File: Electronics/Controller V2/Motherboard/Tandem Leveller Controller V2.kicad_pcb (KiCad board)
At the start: 6 copper layers, 230.5 x 129 mm, 75 parts, among them J1 Conn_01x08, J14 TABLET 1 PWR, J15 TABLET 2 PWR, J2 Conn_01x10, J3 GNSS, J4 TERM, J5 Pulse_J0011D01BNL, J6 CAN, J7 Pulse_J0011D01BNL, J8 776180-1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

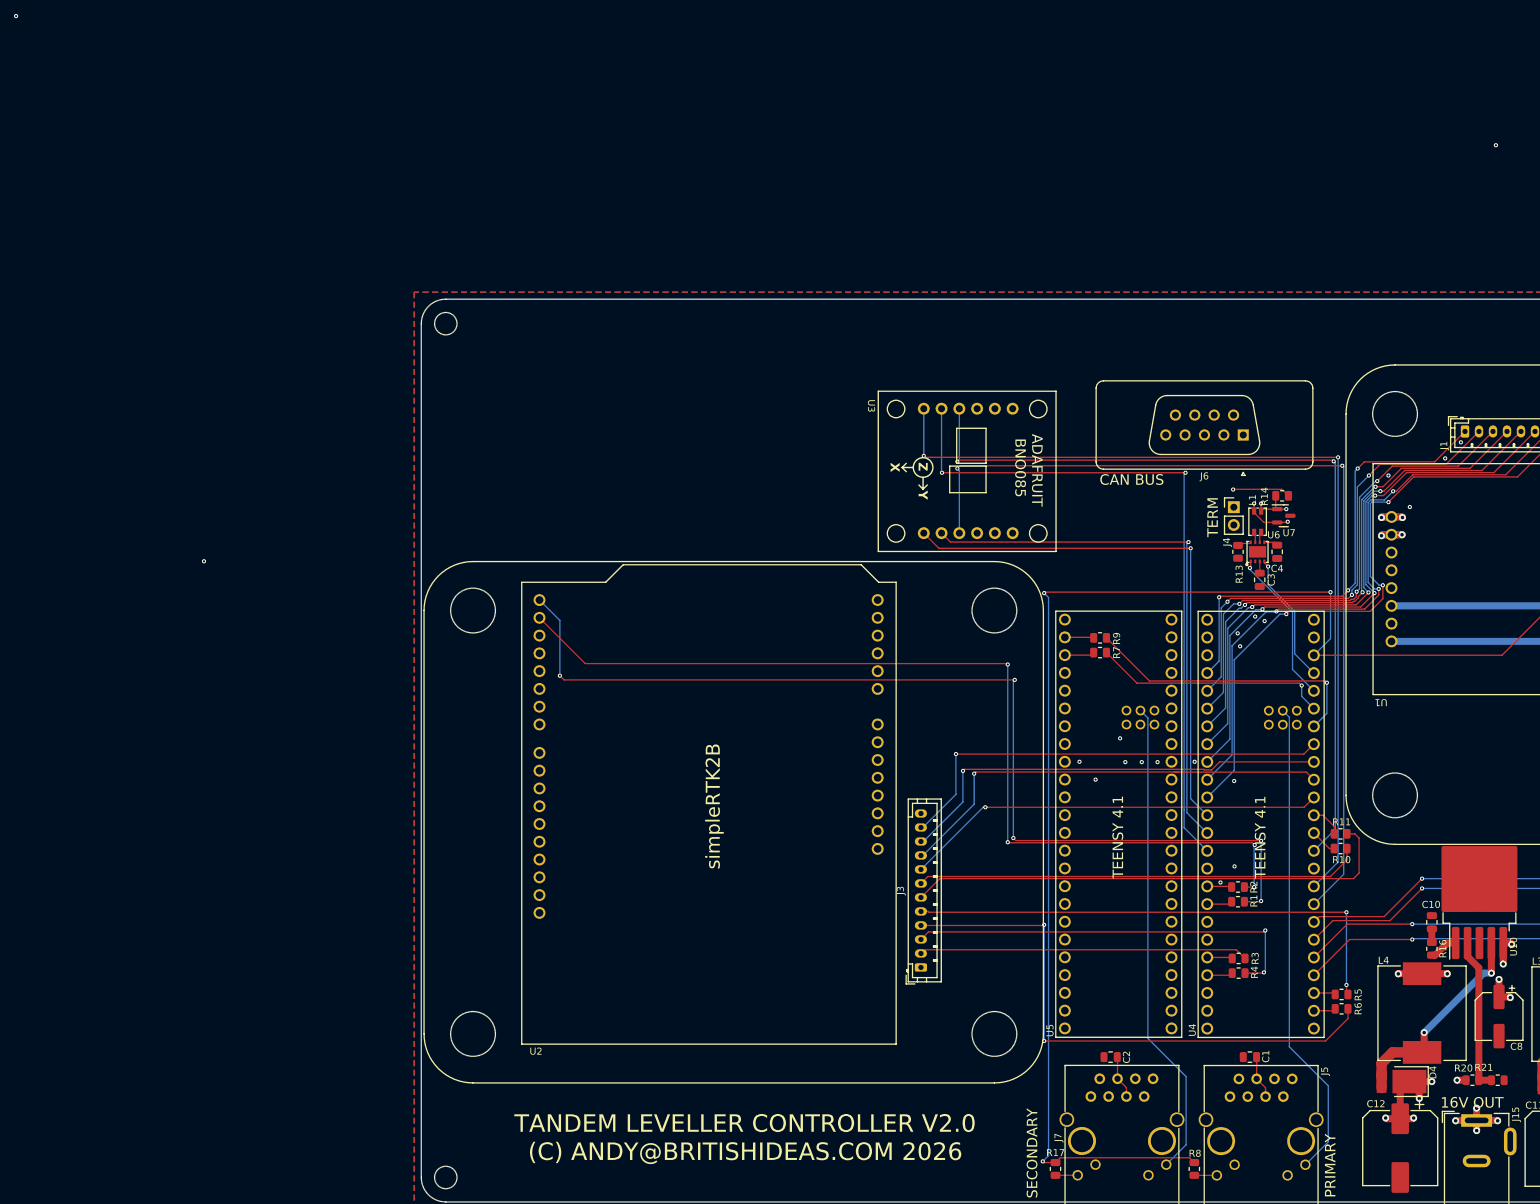
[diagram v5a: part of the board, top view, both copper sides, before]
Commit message: Added generic IMU option.
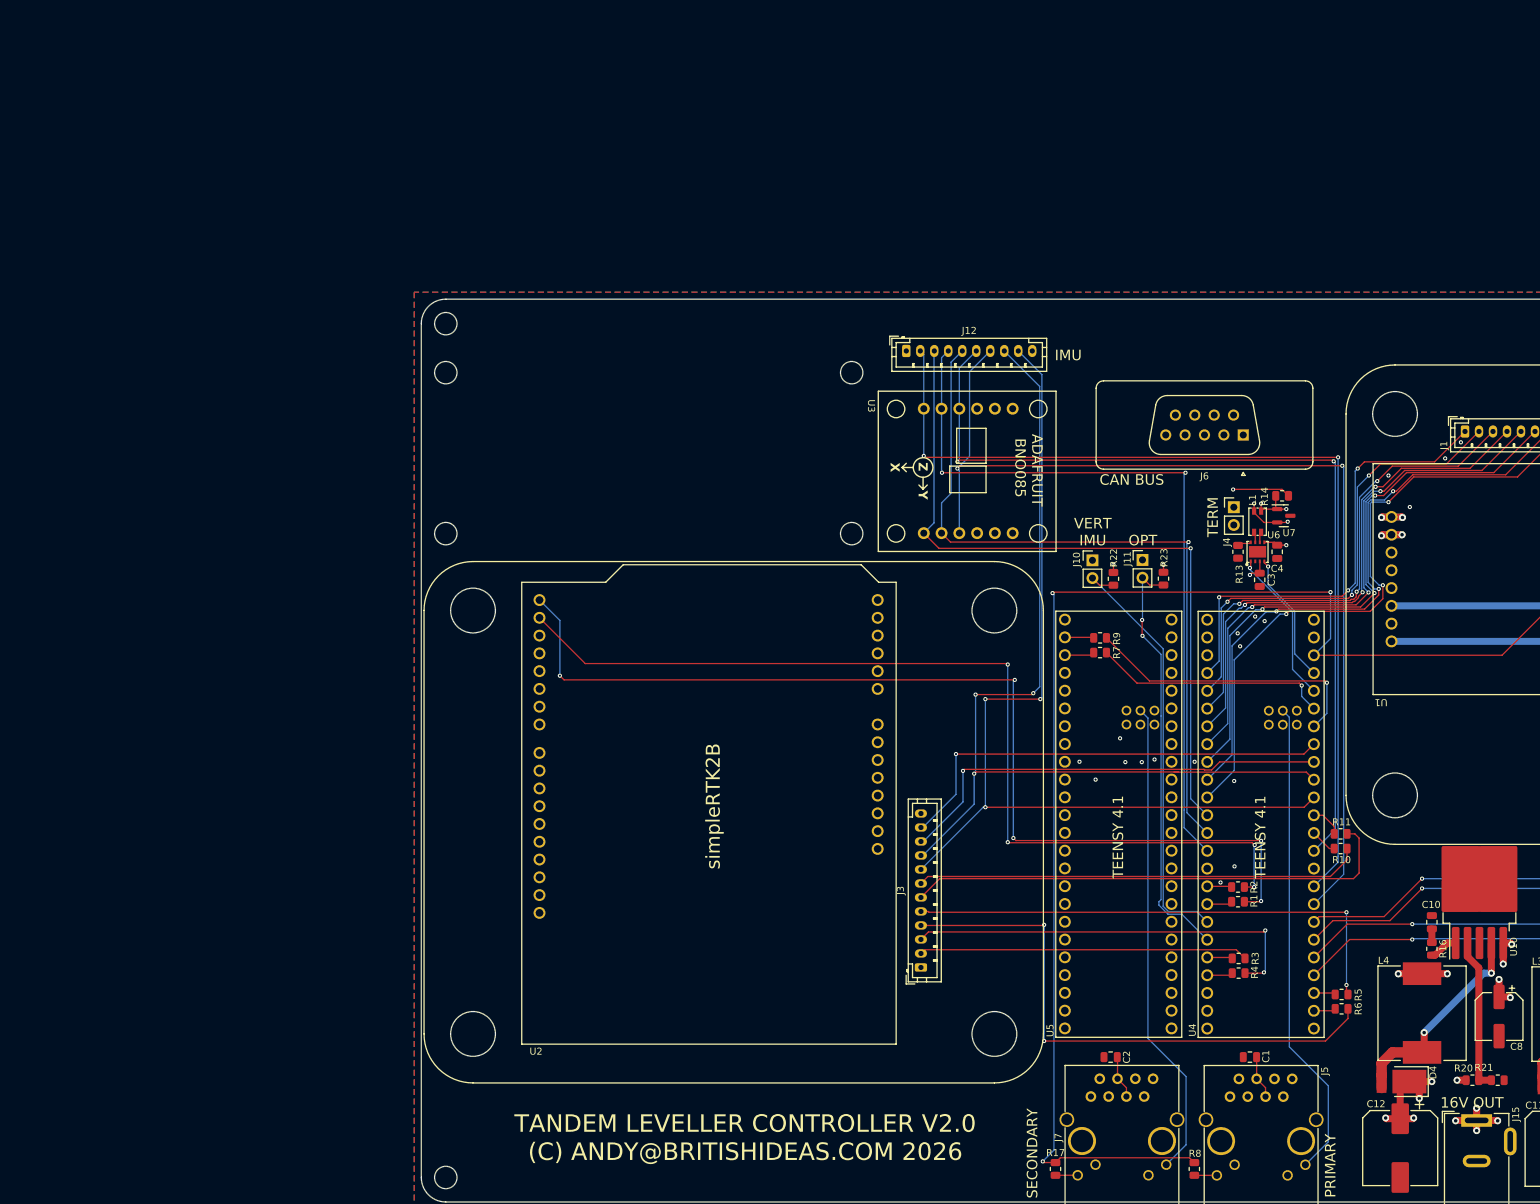
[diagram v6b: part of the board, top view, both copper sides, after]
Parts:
- added H13: MountingHole, MountingHole:MountingHole_3.2mm_M3, F.Cu at (30.5, 34.5)
- added H14: MountingHole, MountingHole:MountingHole_3.2mm_M3, F.Cu at (88.5, 57.5)
- added H15: MountingHole, MountingHole:MountingHole_3.2mm_M3, F.Cu at (30.5, 57.5)
- added H16: MountingHole, MountingHole:MountingHole_3.2mm_M3, F.Cu at (88.5, 34.5)
- added J10: ORIENT, Connector_PinHeader_2.54mm:PinHeader_1x02_P2.54mm_Vertical, F.Cu at (122.9, 61.3)
- added J11: OPT, Connector_PinHeader_2.54mm:PinHeader_1x02_P2.54mm_Vertical, F.Cu at (130.1, 61.3)
- added J12: IMU, Connector_JST:JST_PH_B10B-PH-K_1x10_P2.00mm_Vertical, F.Cu at (96.3, 31.4)
- added R22: 10k, Resistor_SMD:R_0805_2012Metric, F.Cu at (125.9, 64.0)
- added R23: 10k, Resistor_SMD:R_0805_2012Metric, F.Cu at (133.1, 63.9)
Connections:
- U4 pad 18: unconnected-(U4-GPIO26_MOSI1-Pad18) -> Net-(J10-Pin_2)
- U4 pad 19: unconnected-(U4-GPIO27_SCK1-Pad19) -> Net-(J11-Pin_2)
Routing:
- net /GNSS/GPIO_G1: track 60.4 -> 135.0 mm, vias 1 -> 3
- net /GNSS/GPIO_G2: track 64.7 -> 135.8 mm, vias 1 -> 3
- net Net-(J10-Pin_2): track 0.00 -> 61.7 mm
- net Net-(J11-Pin_2): track 0.00 -> 60.4 mm, vias 0 -> 2
- net /IMU/IMU_MOSI: track 78.7 -> 105.9 mm
- net /IMU/~{IMU_CS}: track 78.2 -> 104.8 mm
- net /IMU/~{IMU_RST}: track 129.0 -> 147.7 mm
- net /IMU/IMU_SCK: track 118.6 -> 127.9 mm
- net /IMU/IMU_MISO: track 99.4 -> 108.1 mm
- net /IMU/~{IMU_INT}: track 128.8 -> 137.2 mm
- net +5V: track 12.9 -> 18.0 mm, vias 4 -> 8
- net +3V3: track 271.1 -> 270.0 mm
- net (no net): vias 3 -> 0
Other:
- board text added: "IMU"
- board text added: "OPT"
- board text added: "VERT IMU"
